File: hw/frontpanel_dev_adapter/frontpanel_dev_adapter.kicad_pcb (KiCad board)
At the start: 4 copper layers, 100 x 100 mm, 137 parts, among them J201 KLD-0202-A, J202 Conn_WR-FAST_01x04, J203 Molex_MicroFit_30-43045-0421, J301 FFC_conn_14p, J302 FFC_conn_14p, J303 JST_S2B-PH-SM4-TB, J501 Conn_01x20, J502 Conn_01x20, J503 SWD, J504 STX-3501-3N_(TTL-232R-xV-AJ), J505 Conn_01x03, J601 Conn_02x32_Odd_Even, J602 Conn_02x32_Odd_Even, J603 Conn_02x32_Odd_Even, J604 Conn_02x32_Odd_Even, M101 JLC_tooling_hole, M102 JLC_tooling_hole, M103 JLC_tooling_hole, M401 Fan_4pin, Q201 AO4407A, Q301 AO3400A, Q401 AO3400A, Q501 AO3401A, SW501 SKHUxxE010, U201 TPS54332DDA, U202 TLV1117LV30DCY, U203 TLV1117LV30DCY, U301 TLV9051SIDBV, U401 74LVC2G17gw, U501 STM32F103CBTx, U502 W25Q128JVSIQ, U503 AT24C256C-SSHL, U504 DS3231M, Y501 16MHz

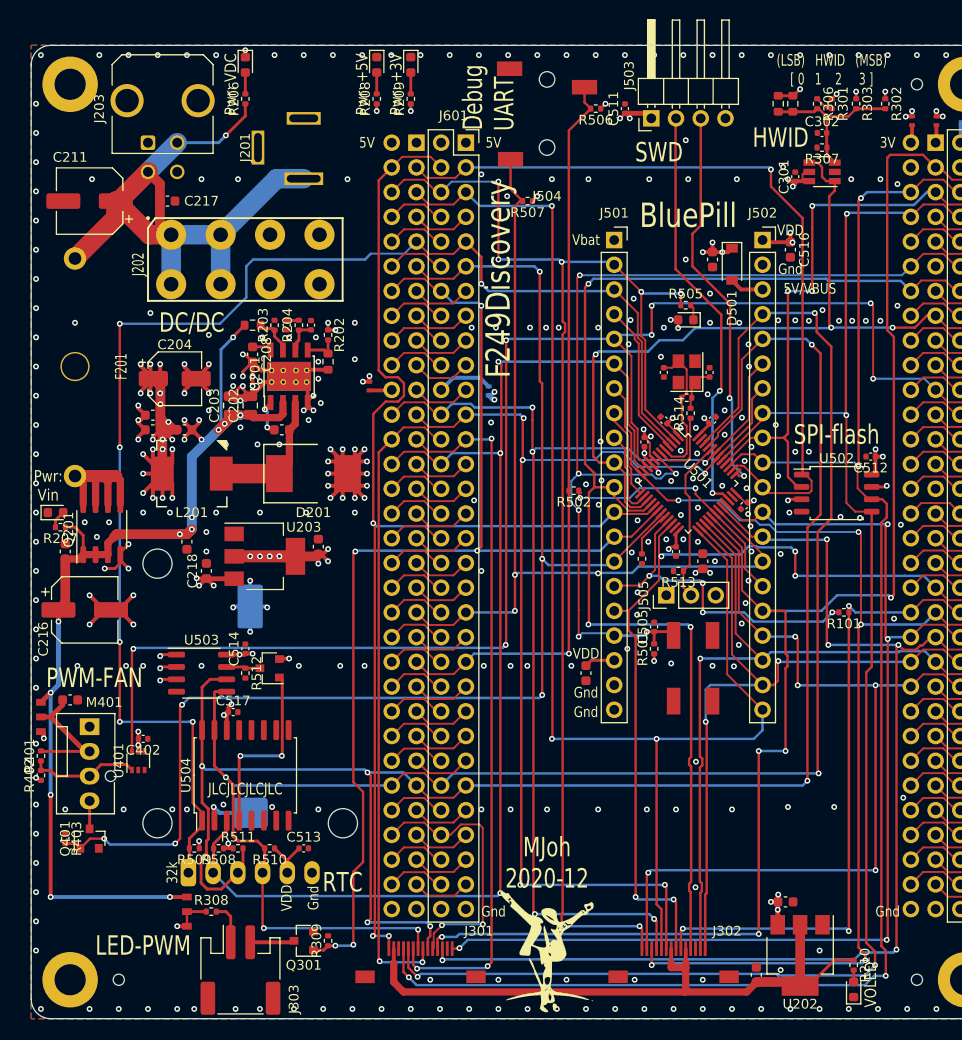
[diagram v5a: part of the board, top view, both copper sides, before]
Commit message: FP adapter board: Added LCSC partnumbers to all components to be PnP:ed; Finalized some silk additions; Generated Gerbers, BoM & pnp-files for JCL assembly
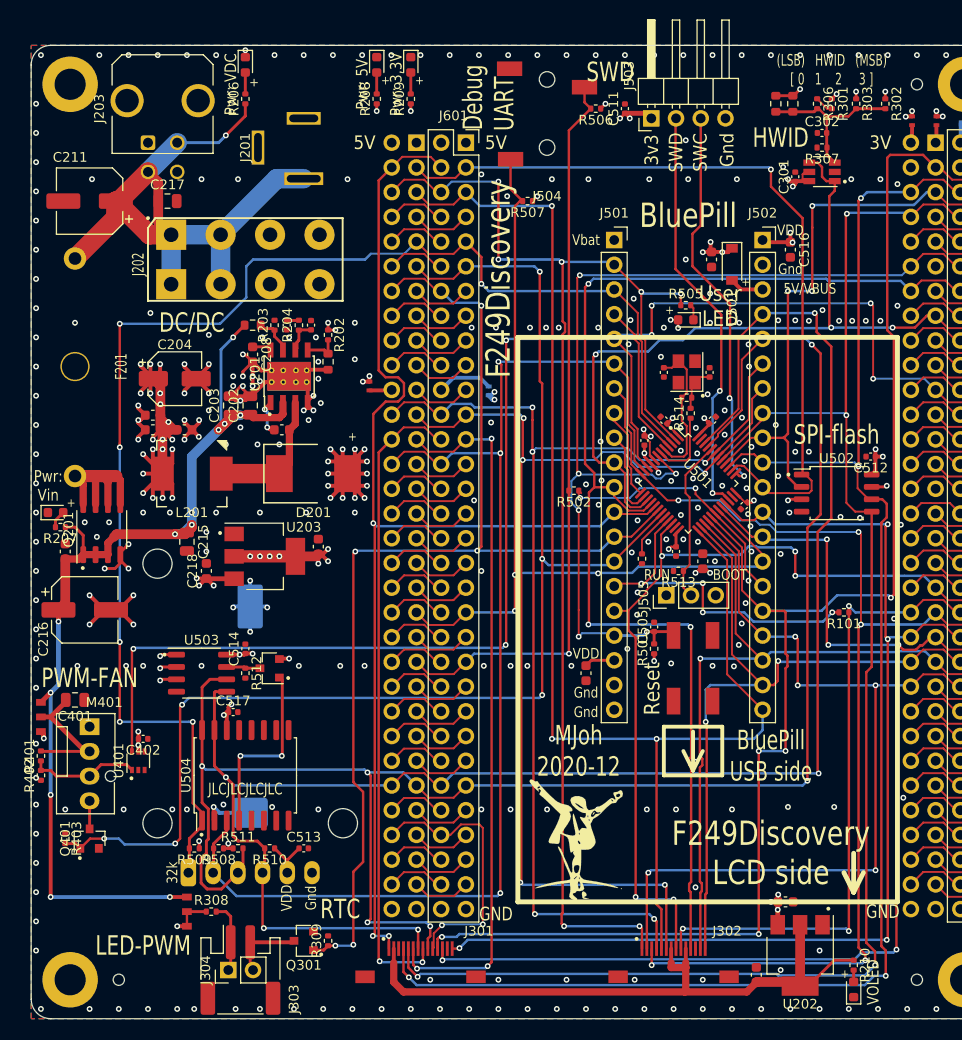
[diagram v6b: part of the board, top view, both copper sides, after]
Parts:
- added J304: Conn_01x02, Connector_PinHeader_2.54mm:PinHeader_1x02_P2.54mm_Vertical, F.Cu at (70.2, 145.0)
- C215, C217, C401: footprint Capacitor_SMD:C_0603_1608Metric -> Capacitor_SMD:C_0805_2012Metric
- moved Logo101 11.9 mm to (106.0, 131.5)
- moved C401 0.50 mm to (54.5, 117.2)
- moved R305 0.25 mm to (126.5, 56.0)
- moved C502 0.15 mm to (113.0, 90.6)
- moved C510 0.10 mm to (119.9, 72.0)
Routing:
- net Net-(J303-Pad2): track 4.56 -> 7.53 mm
- net Net-(J303-Pad1): track 4.35 -> 7.30 mm
- net /MCU / Bluepill/USART3_TX: track 34.1 -> 34.8 mm
- net VIN: track 105.4 -> 106.0 mm
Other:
- rule pad_to_mask_clearance: 0.05 -> 0
- board text added: "+"
- board text added: "3.3V"
- board text added: "3v3"
- board text added: "BOOT"
- board text added: "BluePill USB side"
- board text added: "F249Discovery LCD side"
- board text added: "GND"
- board text added: "Pwr: 3,3V"
- board text added: "Pwr: 5V"
- board text added: "RUN"
- board text added: "Reset"
- board text added: "SWC"
- board text added: "SWCK"
- board text added: "SWDT"
- board text added: "User LED"
- board text removed: "Pwr: +3V"
- board text removed: "Pwr: +5V"
